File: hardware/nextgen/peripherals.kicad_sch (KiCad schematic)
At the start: 34 parts, among them J10 SM04B-SRSS-TB, J11 U254-051T-4BH81-S2S, J3 UDPI, J3 UEXT, J5 XKTF-0803-0, Q1 BSS138, SW2 PROG_EN, U3 PCF8563T, U7 CH340C, Y1 32kHz

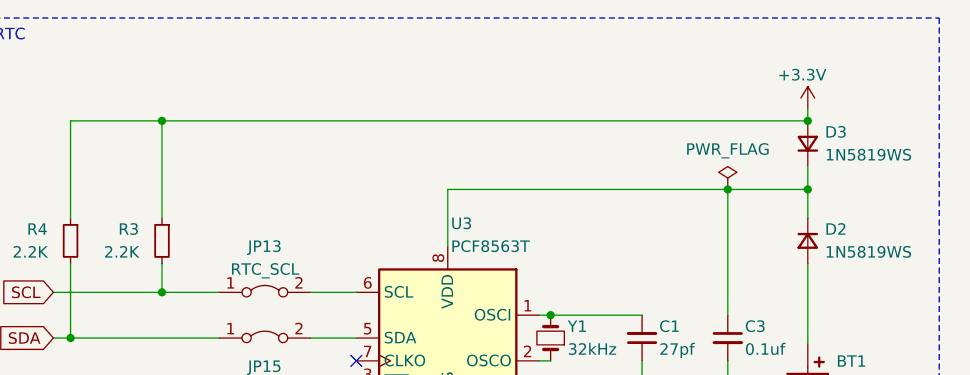
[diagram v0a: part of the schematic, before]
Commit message: Reorganize hardware directories
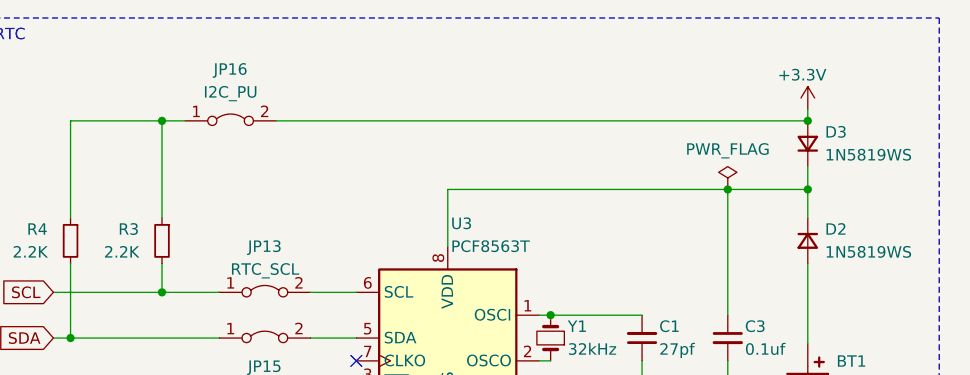
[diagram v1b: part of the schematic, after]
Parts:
- added JP16: I2C_PU, Jumper:SolderJumper-2_P1.3mm_Bridged_RoundedPad1.0x1.5mm, symbol Jumper:Jumper_2_Bridged
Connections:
- net +3.3V: now also JP16.2 (B); no longer R3.1, R4.1
- new net: JP16.1 (A), R3.1, R4.1
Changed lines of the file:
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@@
   (junction (at 82.55 42.545) (diameter 0) (color 0 0 0 0)
   )
+  (junction (at 179.07 34.925) (diameter 0) (color 0 0 0 0)
+  )
   (junction (at 237.49 78.74) (diameter 0) (color 0 0 0 0)
   )
@@
   )
   (junction (at 74.93 42.545) (diameter 0) (color 0 0 0 0)
-  )
-  (junction (at 179.07 34.925) (diameter 0) (color 0 0 0 0)
   )
   (junction (at 74.93 62.23) (diameter 0) (color 0 0 0 0)
@@
     (stroke (width 0) (type default))
   )
+  (wire (pts (xy 168.91 34.925) (xy 179.07 34.925))
+    (stroke (width 0) (type default))
+  )
   (wire (pts (xy 222.25 56.515) (xy 232.41 56.515))
     (stroke (width 0) (type default))
@@
     (stroke (width 0) (type default))
   )
+  (wire (pts (xy 179.07 34.925) (xy 181.61 34.925))
+    (stroke (width 0) (type default))
+  )
   (wire (pts (xy 123.19 78.74) (xy 123.19 77.47))
     (stroke (width 0) (type default))
@@
     (stroke (width 0) (type default))
   )
+  (wire (pts (xy 191.77 34.925) (xy 250.825 34.925))
+    (stroke (width 0) (type default))
+  )
   (wire (pts (xy 161.925 128.905) (xy 161.925 132.715))
     (stroke (width 0) (type default))
@@
     (stroke (width 0) (type default))
   )
+  (wire (pts (xy 168.91 34.925) (xy 168.91 45.72))
+    (stroke (width 0) (type default))
+  )
   (wire (pts (xy 210.82 42.545) (xy 210.82 48.895))
     (stroke (width 0) (type default))
@@
     (stroke (width 0) (type default))
   )
+  (wire (pts (xy 74.93 48.895) (xy 74.93 62.23))
+    (stroke (width 0) (type default))
+  )
+  (wire (pts (xy 118.11 77.47) (xy 118.11 78.74))
+    (stroke (width 0) (type default))
+  )
+  (wire (pts (xy 248.285 135.255) (xy 251.46 135.255))
+    (stroke (width 0) (type default))
+  )
+  (wire (pts (xy 109.22 139.065) (xy 101.6 139.065))
+    (stroke (width 0) (type default))
+  )
+  (wire (pts (xy 74.93 42.545) (xy 82.55 42.545))
+    (stroke (width 0) (type default))
+  )
+  (wire (pts (xy 158.75 131.445) (xy 164.465 131.445))
+    (stroke (width 0) (type default))
+  )
+  (wire (pts (xy 66.675 42.545) (xy 66.675 43.815))
+    (stroke (width 0) (type default))
+  )
   (wire (pts (xy 179.07 34.925) (xy 179.07 45.72))
     (stroke (width 0) (type default))
   )
-  (wire (pts (xy 74.93 48.895) (xy 74.93 62.23))
-    (stroke (width 0) (type default))
-  )
-  (wire (pts (xy 118.11 77.47) (xy 118.11 78.74))
-    (stroke (width 0) (type default))
-  )
-  (wire (pts (xy 248.285 135.255) (xy 251.46 135.255))
-    (stroke (width 0) (type default))
-  )
-  (wire (pts (xy 109.22 139.065) (xy 101.6 139.065))
-    (stroke (width 0) (type default))
-  )
-  (wire (pts (xy 74.93 42.545) (xy 82.55 42.545))
-    (stroke (width 0) (type default))
-  )
-  (wire (pts (xy 158.75 131.445) (xy 164.465 131.445))
-    (stroke (width 0) (type default))
-  )
-  (wire (pts (xy 66.675 42.545) (xy 66.675 43.815))
-    (stroke (width 0) (type default))
-  )
   (wire (pts (xy 66.675 42.545) (xy 74.93 42.545))
     (stroke (width 0) (type default))
@@
     (stroke (width 0) (type default))
   )
-  (wire (pts (xy 179.07 34.925) (xy 250.825 34.925))
-    (stroke (width 0) (type default))
-  )
   (wire (pts (xy 198.755 135.89) (xy 201.295 135.89))
     (stroke (width 0) (type default))
   )
-  (wire (pts (xy 168.91 34.925) (xy 179.07 34.925))
-    (stroke (width 0) (type default))
-  )
   (wire (pts (xy 100.965 119.38) (xy 102.235 119.38))
     (stroke (width 0) (type default))
@@
   )
   (wire (pts (xy 179.07 50.8) (xy 179.07 53.975))
-    (stroke (width 0) (type default))
-  )
-  (wire (pts (xy 168.91 34.925) (xy 168.91 45.72))
     (stroke (width 0) (type default))
   )
@@
         )
       )
+    )
+  )
+  (symbol (lib_id "Jumper:Jumper_2_Bridged") (at 186.69 34.925 0) (unit 1)
+    (in_bom yes) (on_board yes) (dnp no) (fields_autoplaced)
+    (property "Reference" "JP16" (at 186.69 29.21 0)
+      (effects (font (size 1.27 1.27)))
+    )
+    (property "Value" "I2C_PU" (at 186.69 31.75 0)
+      (effects (font (size 1.27 1.27)))
+    )
+    (property "Footprint" "Jumper:SolderJumper-2_P1.3mm_Bridged_RoundedPad1.0x1.5mm" (at 186.69 34.925 0)
+      (effects (font (size 1.27 1.27)) hide)
+    )
+    (property "Datasheet" "~" (at 186.69 34.925 0)
+      (effects (font (size 1.27 1.27)) hide)
+    )
+    (pin "1")
+    (pin "2")
+    (instances
+      (project "z80ctrlng"
+        (path "/9c261024-c69f-48e3-a573-d08c538d0e71/5cf77197-9b78-4e84-b90a-802a333be582"
+          (reference "JP16") (unit 1)
+        )
+      )

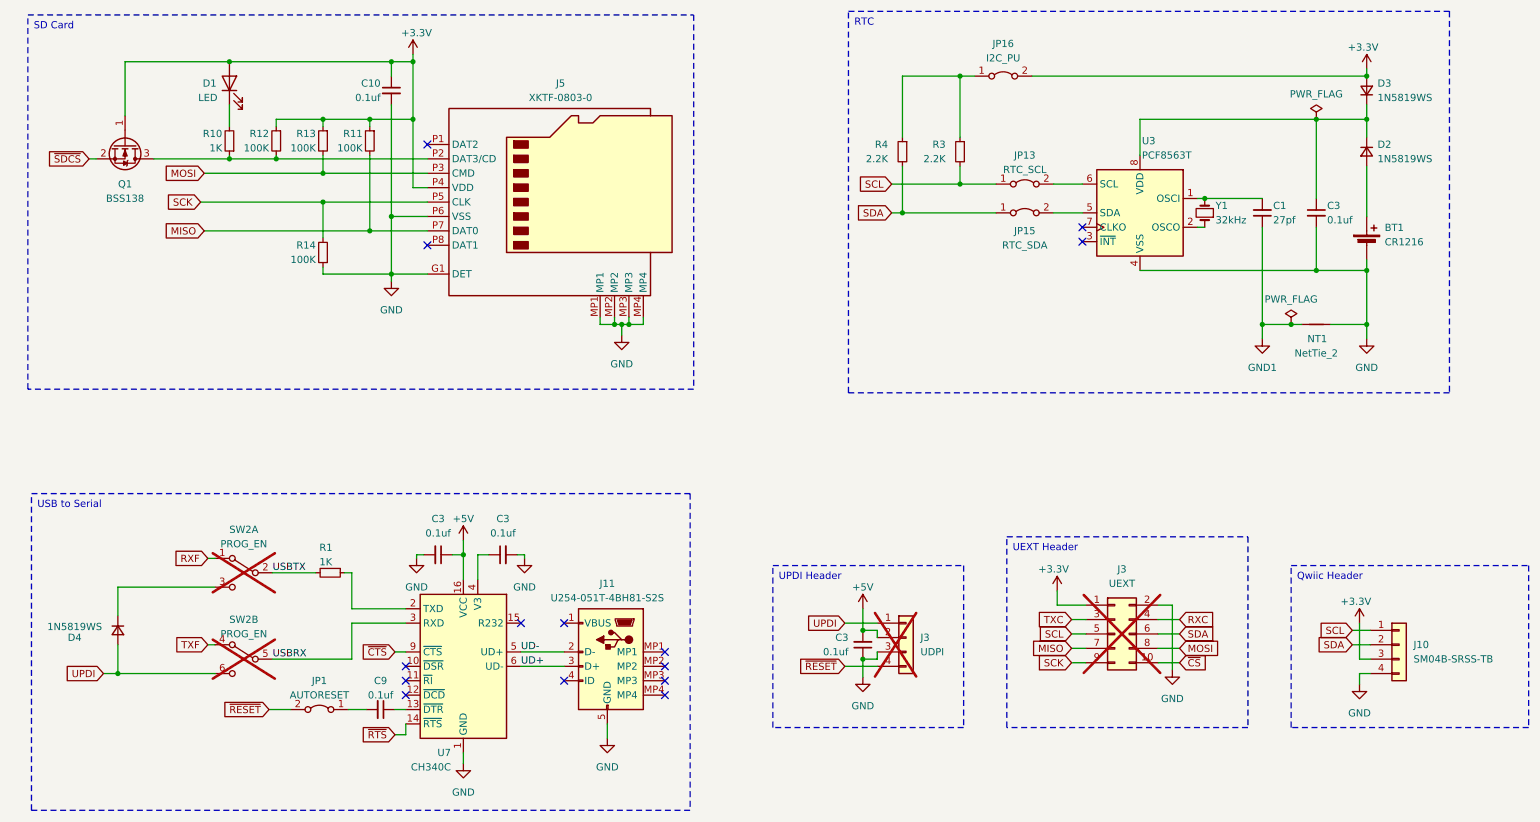
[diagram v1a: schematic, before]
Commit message: Get rid of serial bus links, make banking software controllable
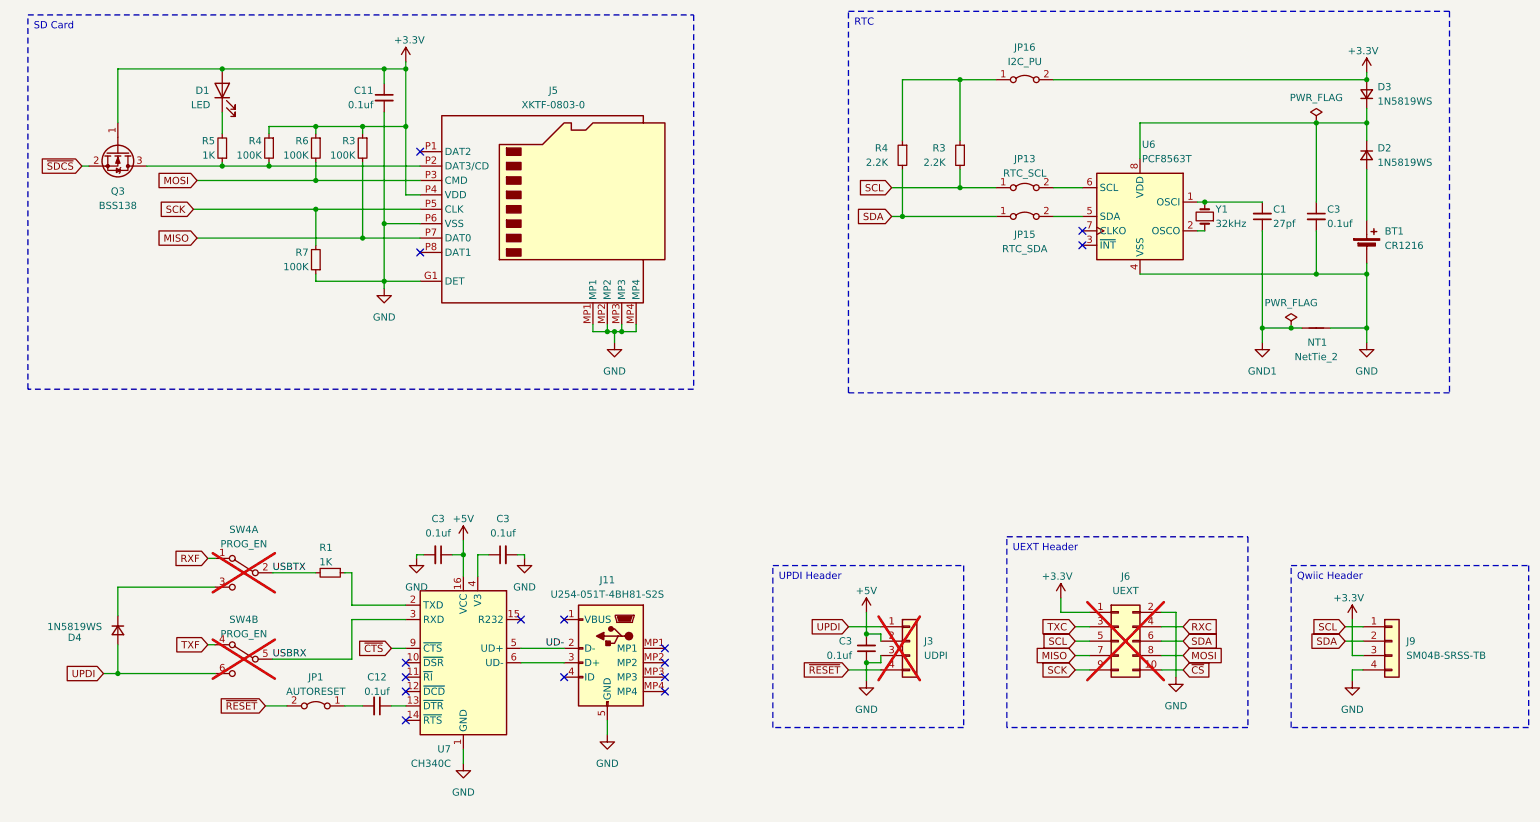
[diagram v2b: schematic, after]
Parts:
- renumbered C10 to C11, C9 to C12, J3 to J6, J10 to J9, Q1 to Q3, R11 to R3, R12 to R4, R10 to R5, R13 to R6, R14 to R7, SW2 to SW4, U3 to U6
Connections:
- net UD+: no longer names the net of J11.3 (D+), U7.6 (UD-)
- net ~{RTS}: no longer names the net of U7.14 (~{RTS})
- no-connect marks 14 -> 15
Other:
- moved on the sheet: BT1, C1, C11, C12, C3, D1, D2, D3, J11, J3, J5, J6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
